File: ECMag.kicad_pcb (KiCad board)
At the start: 2 copper layers, 48 parts, among them J1 Conn_01x12, J2 Conn_01x05, J3 Conn_01x04, J4 USB_B, J5 Barrel_Jack_SW, J6 Conn_01x04, K1 Tactil Switch NA, K2 Tactil Switch B3F NA, K3 Tactil Switch NA, K4 Tactil Switch NA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

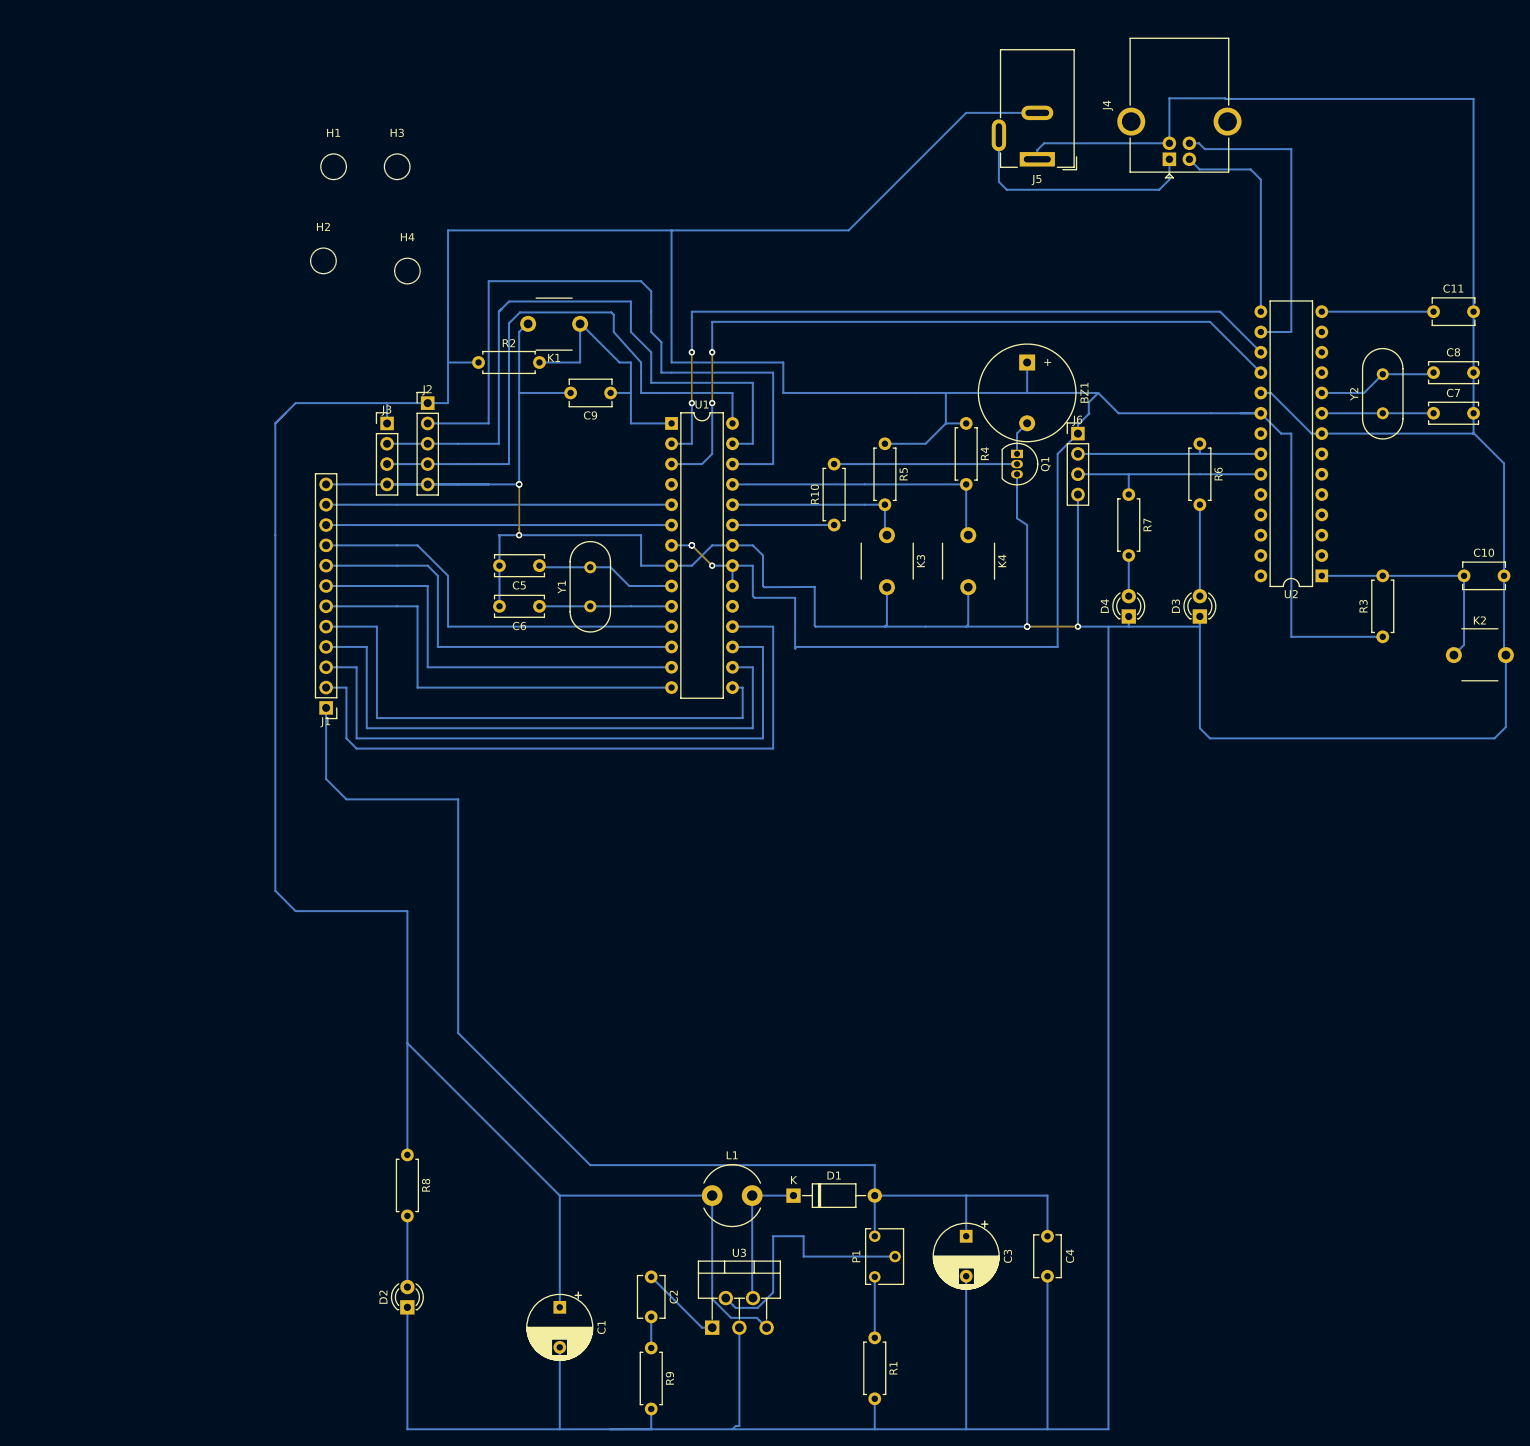
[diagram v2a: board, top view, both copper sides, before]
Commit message: Correcciones faltantes indicadas por el profesor
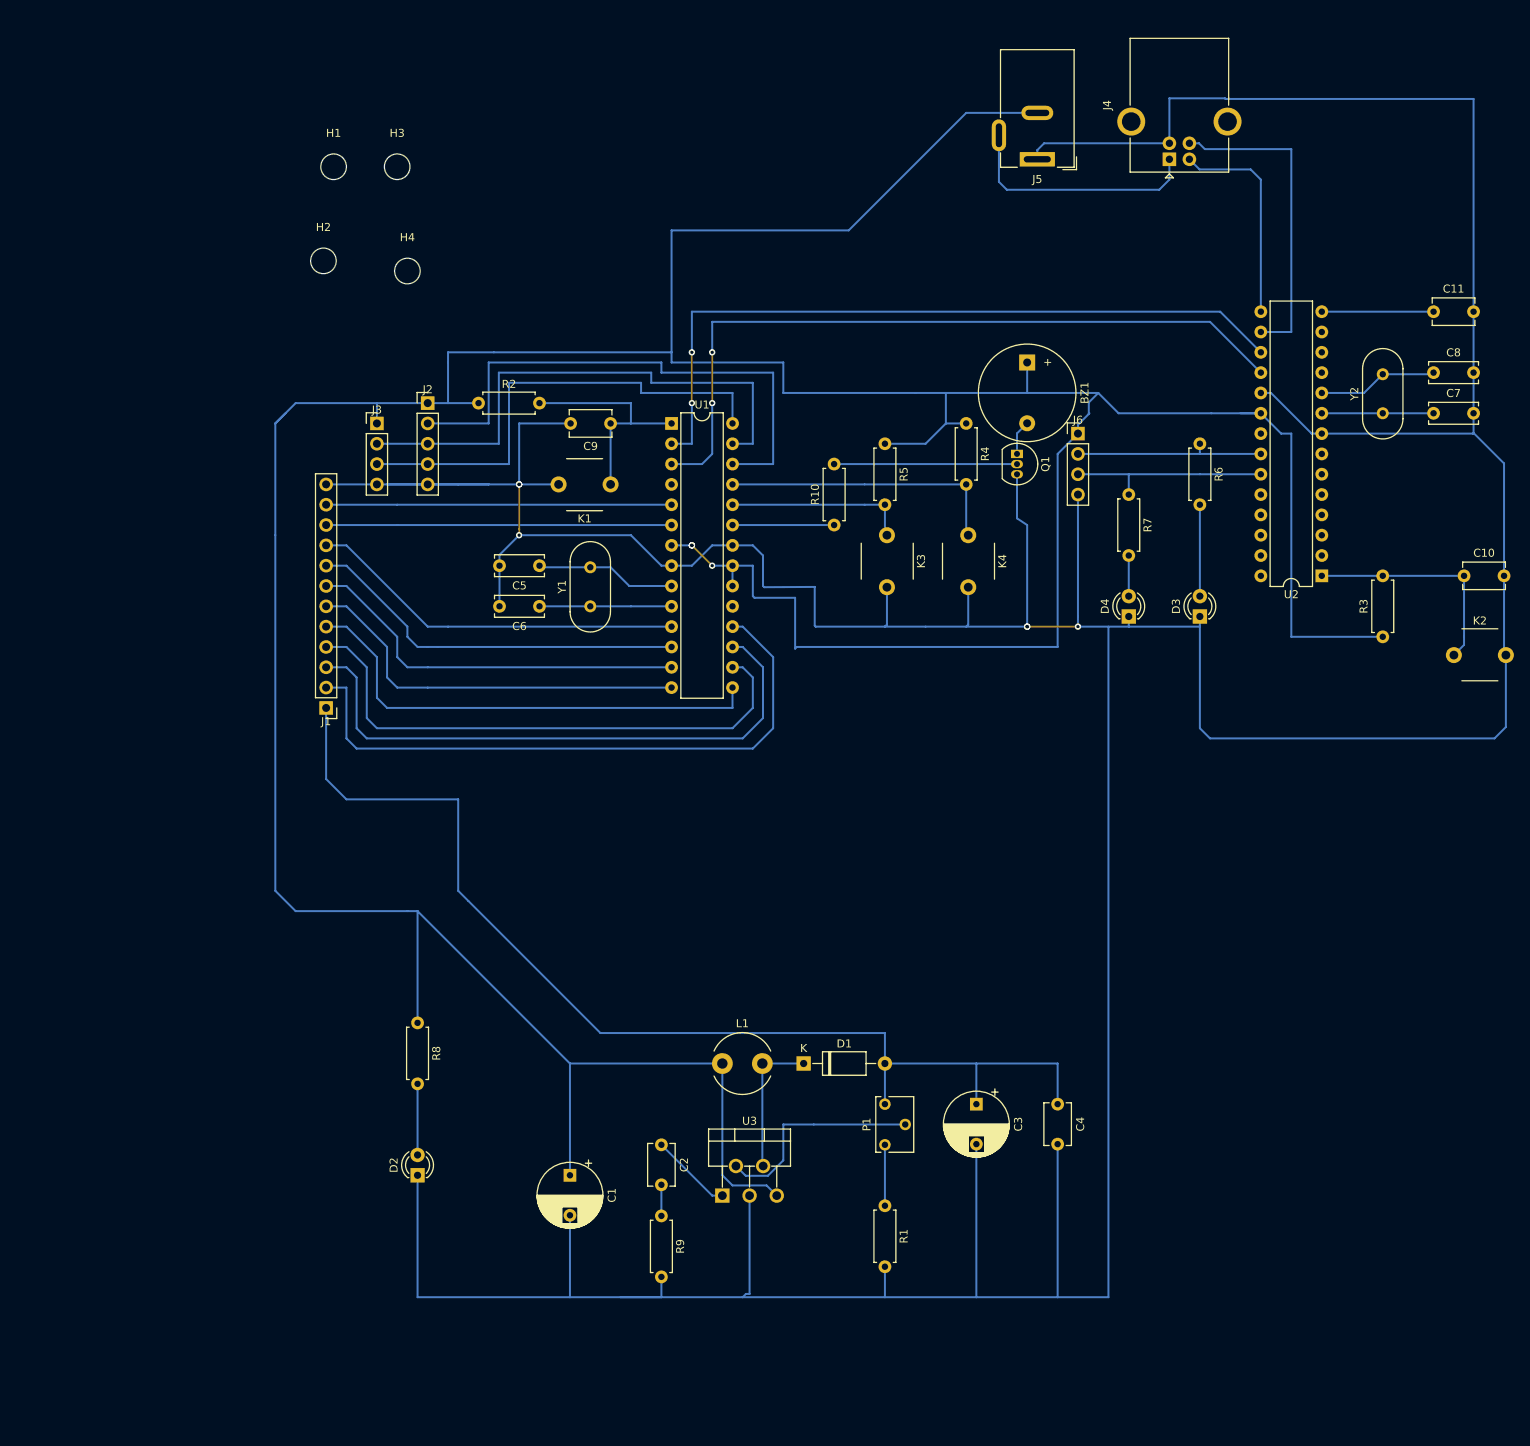
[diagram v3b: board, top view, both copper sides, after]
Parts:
- moved K1 20.4 mm to (106.7, 77.2)
- moved C1 16.6 mm to (101.6, 161.3)
- moved C2 16.6 mm to (113.0, 157.5)
- moved D1 16.6 mm to (130.8, 147.3)
- moved D2 16.6 mm to (82.5, 161.3)
- moved L1 16.6 mm to (120.7, 147.3)
- moved R1 16.6 mm to (141.0, 165.1)
- moved C3 16.6 mm to (152.4, 152.4)
- moved C4 16.6 mm to (162.6, 152.4)
- moved P1 16.6 mm to (141.0, 152.4)
- moved R8 16.6 mm to (82.5, 142.2)
- moved R9 16.6 mm to (113.0, 166.4)
- moved U3 16.6 mm to (120.7, 163.8)
- moved R2 5.08 mm to (90.2, 64.8)
- moved C9 3.81 mm to (106.7, 67.3)
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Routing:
- net +5V: track 574.0 -> 544.1 mm
- net GND: track 729.1 -> 699.5 mm
- net /DRDY: track 87.4 -> 68.6 mm
- net +12V: track 155.2 -> 139.2 mm
- net /SDA: track 82.1 -> 67.3 mm
- net /SCL: track 72.9 -> 59.7 mm
- net /a4: track 68.6 -> 60.5 mm
- net Net-(P1-Pad2): track 32.0 -> 27.0 mm
- net /a6: track 53.3 -> 48.9 mm
- net /a2: track 78.7 -> 74.3 mm
- net /a7: track 52.6 -> 48.1 mm
- net /a3: track 73.7 -> 69.2 mm
- net Net-(C9-Pad1): track 33.5 -> 29.2 mm
- net /a1: track 83.1 -> 79.4 mm
- net /a5: track 53.3 -> 49.6 mm
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
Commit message: primera versión del pcb
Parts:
- K1, K3, K4: value Tactil Switch NA -> Tactil Switch B3F NA
- K2: value Tactil Switch B3F NA -> Switch B3F NA
- U1: value ATmega328P-PU -> ATMega328
- U2: value PIC18F2550-ISO -> PIC18F2550
- moved H1 140.5 mm to (193.0, 106.7)
- moved H3 114.5 mm to (193.0, 53.3)
- moved R9 88.7 mm to (152.4, 86.9), turned to 90 degrees
- moved D2 88.7 mm to (125.7, 83.8), turned to 270 degrees
- moved C2 81.6 mm to (161.0, 91.4), turned to 90 degrees
- moved U3 80.7 mm to (156.2, 91.4), turned to 180 degrees
- moved R1 80.2 mm to (172.7, 91.4), turned to 0 degrees
- moved C1 71.6 mm to (132.1, 96.5), turned to 90 degrees
- moved C3 67.6 mm to (190.5, 96.5), turned to 90 degrees
- moved P1 62.5 mm to (168.9, 96.5), turned to 270 degrees
- moved R8 62.0 mm to (125.7, 97.8), turned to 90 degrees
- moved C4 59.9 mm to (184.2, 96.5), turned to 90 degrees
- moved L1 59.9 mm to (142.2, 91.4), turned to 270 degrees
- moved H4 58.8 mm to (87.6, 106.7)
- moved D1 56.0 mm to (161.3, 100.3)
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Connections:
- U1 pad 11: /a8 -> /a7
- U1 pad 12: /a7 -> /a5
- U1 pad 13: /a6 -> /a3
- U1 pad 14: /a5 -> /a1
- U1 pad 15: /a4 -> /a2
- U1 pad 16: /a3 -> /a4
- U1 pad 17: /a2 -> /a6
- U1 pad 18: /a1 -> /a8
- U1 pad 19: Net-(U1-Pad19) -> (no net)
- U1 pad 4: Net-(U1-Pad4) -> (no net)
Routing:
- net GND: track 699.5 -> 351.0 mm, vias 6 -> 0
- net +5V: track 544.1 -> 253.2 mm, vias 3 -> 0
- net /a1: track 79.4 -> 26.5 mm
- net /a3: track 69.2 -> 27.5 mm
- net /a2: track 74.3 -> 35.1 mm
- net +12V: track 139.2 -> 111.6 mm
- net /DRDY: track 68.6 -> 41.3 mm
- net /a4: track 60.5 -> 36.2 mm
- net /SDA: track 67.3 -> 43.3 mm
- net /SCL: track 59.7 -> 37.1 mm
- net /D+: track 39.7 -> 17.3 mm
- net /a5: track 49.6 -> 28.6 mm
- net /TxRx: track 93.3 -> 73.6 mm
- net /RxTx: track 92.3 -> 72.9 mm
- net /a7: track 48.1 -> 29.6 mm
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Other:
- board outline added: 113 x 61 mm

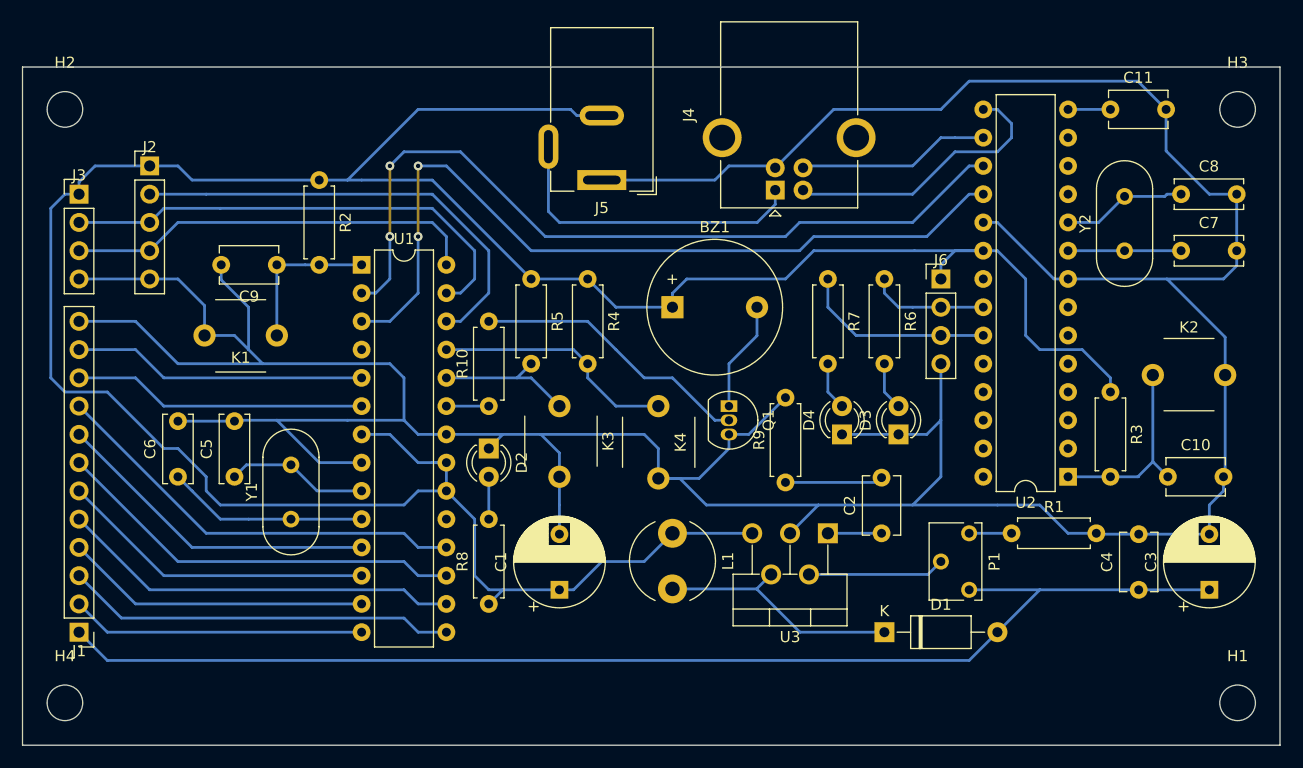
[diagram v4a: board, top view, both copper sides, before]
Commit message: cambio de huellas del pulsador
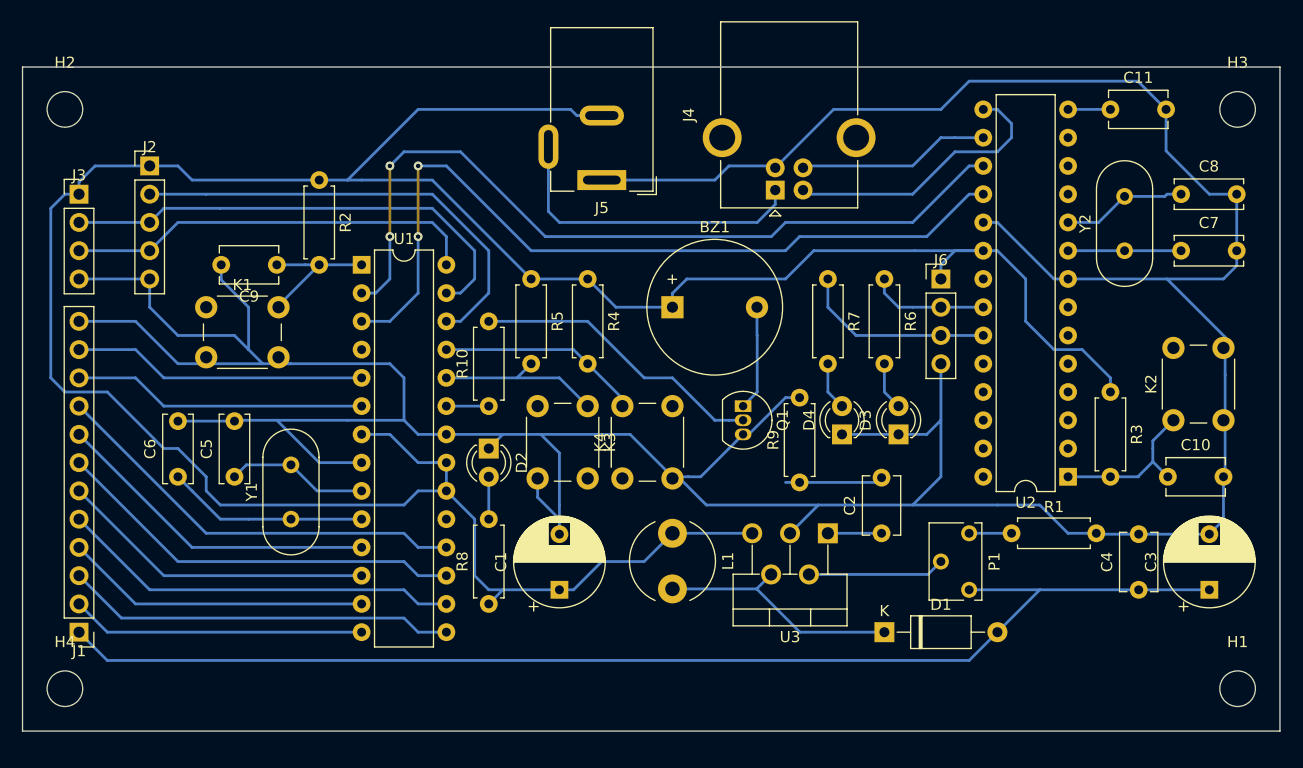
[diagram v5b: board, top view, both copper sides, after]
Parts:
- K1, K3, K4: footprint EMS_huellas:SW_6x5mm_2C -> Button_Switch_THT:SW_PUSH_6mm_H5mm
- K2: value Switch B3F NA -> Tactil Switch B3F NA; footprint EMS_huellas:SW_6x5mm_2C -> Button_Switch_THT:SW_PUSH_6mm_H5mm
- moved K4 7.26 mm to (137.7, 86.5), turned to 90 degrees
- moved K1 6.84 mm to (100.3, 71.1), turned to 0 degrees
- moved K2 6.61 mm to (187.3, 81.3), turned to 90 degrees
- moved K3 2.54 mm to (134.6, 80.0)
- moved H1 1.27 mm to (193.0, 105.4)
- moved H4 1.27 mm to (87.6, 105.4)
- moved Q1 1.27 mm to (148.6, 80.0)
- moved R9 1.27 mm to (153.7, 86.9)
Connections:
- U2 pad 11: Net-(U2-Pad11) -> (no net)
- U2 pad 12: Net-(U2-Pad12) -> (no net)
- U2 pad 13: Net-(U2-Pad13) -> (no net)
- U2 pad 2: Net-(U2-Pad2) -> (no net)
- U2 pad 21: Net-(U2-Pad21) -> (no net)
- U2 pad 24: Net-(U2-Pad24) -> (no net)
- U2 pad 25: Net-(U2-Pad25) -> (no net)
- U2 pad 26: Net-(U2-Pad26) -> (no net)
- U2 pad 27: Net-(U2-Pad27) -> (no net)
- U2 pad 28: Net-(U2-Pad28) -> (no net)
- U2 pad 3: Net-(U2-Pad3) -> (no net)
- U2 pad 4: Net-(U2-Pad4) -> (no net)
- U2 pad 5: Net-(U2-Pad5) -> (no net)
- U2 pad 6: Net-(U2-Pad6) -> (no net)
- U2 pad 7: Net-(U2-Pad7) -> (no net)
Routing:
- net /Btn_NL: track 21.9 -> 18.2 mm
- net Net-(C10-Pad1): track 18.0 -> 14.7 mm
- net /Btn_ND: track 13.0 -> 15.5 mm
- net GND: track 351.0 -> 353.1 mm
- net Net-(Q1-Pad2): track 25.3 -> 26.5 mm
- net +5V: track 253.2 -> 252.5 mm
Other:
- board size 113 x 61 mm -> 113 x 59.7 mm

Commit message: Arreglo de F.Silks y F.Fab
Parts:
- K1, K2, K3, K4: value Tactil Switch B3F NA -> Switch
- moved H1 105.4 mm to (87.6, 105.4)
- moved H4 105.4 mm to (193.0, 105.4)
- moved R5 2.54 mm to (132.1, 68.6)
- moved R4 2.54 mm to (137.2, 68.6)
- moved R10 1.27 mm to (127.0, 80.0)
- moved R8 1.27 mm to (127.0, 97.8)
- moved C1 1.27 mm to (133.3, 96.5)
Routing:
- net GND: track 353.1 -> 363.1 mm
- net Net-(C10-Pad1): track 14.7 -> 21.2 mm
- net /Btn_NL: track 18.2 -> 20.7 mm
- net Net-(Q1-Pad2): track 26.5 -> 25.3 mm
- net /Bzz: track 3.81 -> 5.08 mm
- net Net-(C2-Pad2): track 8.81 -> 7.54 mm
- net +5V: track 252.5 -> 251.7 mm
- net Net-(D2-Pad2): track 3.81 -> 4.34 mm
